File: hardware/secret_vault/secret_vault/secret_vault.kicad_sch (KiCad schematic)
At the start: 13 parts

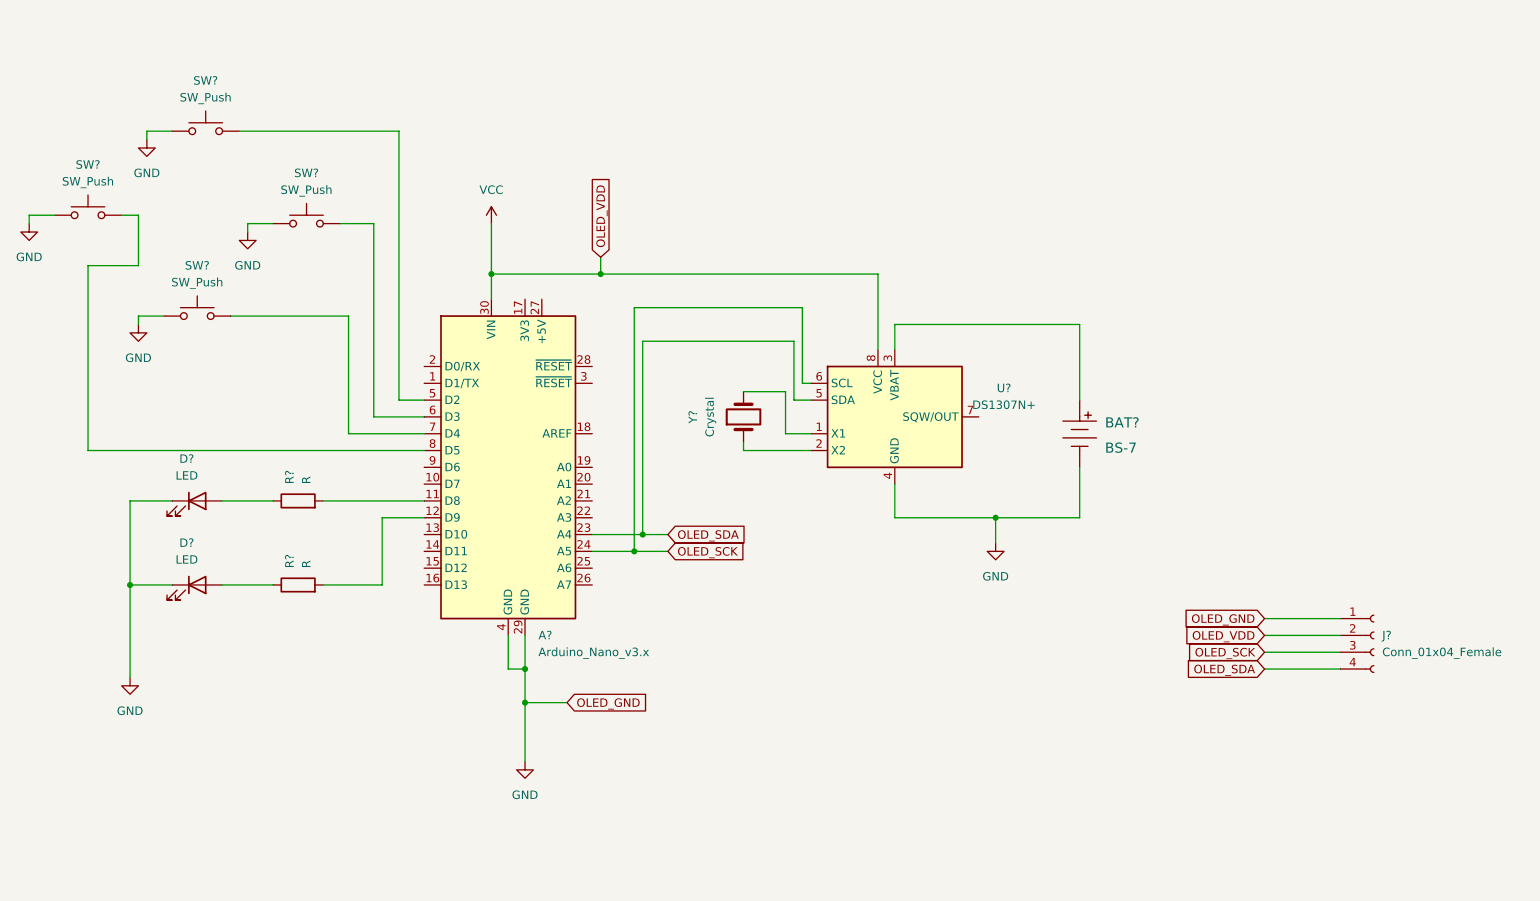
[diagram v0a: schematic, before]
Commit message: Updated PCB board and sent it to OSH park for fab
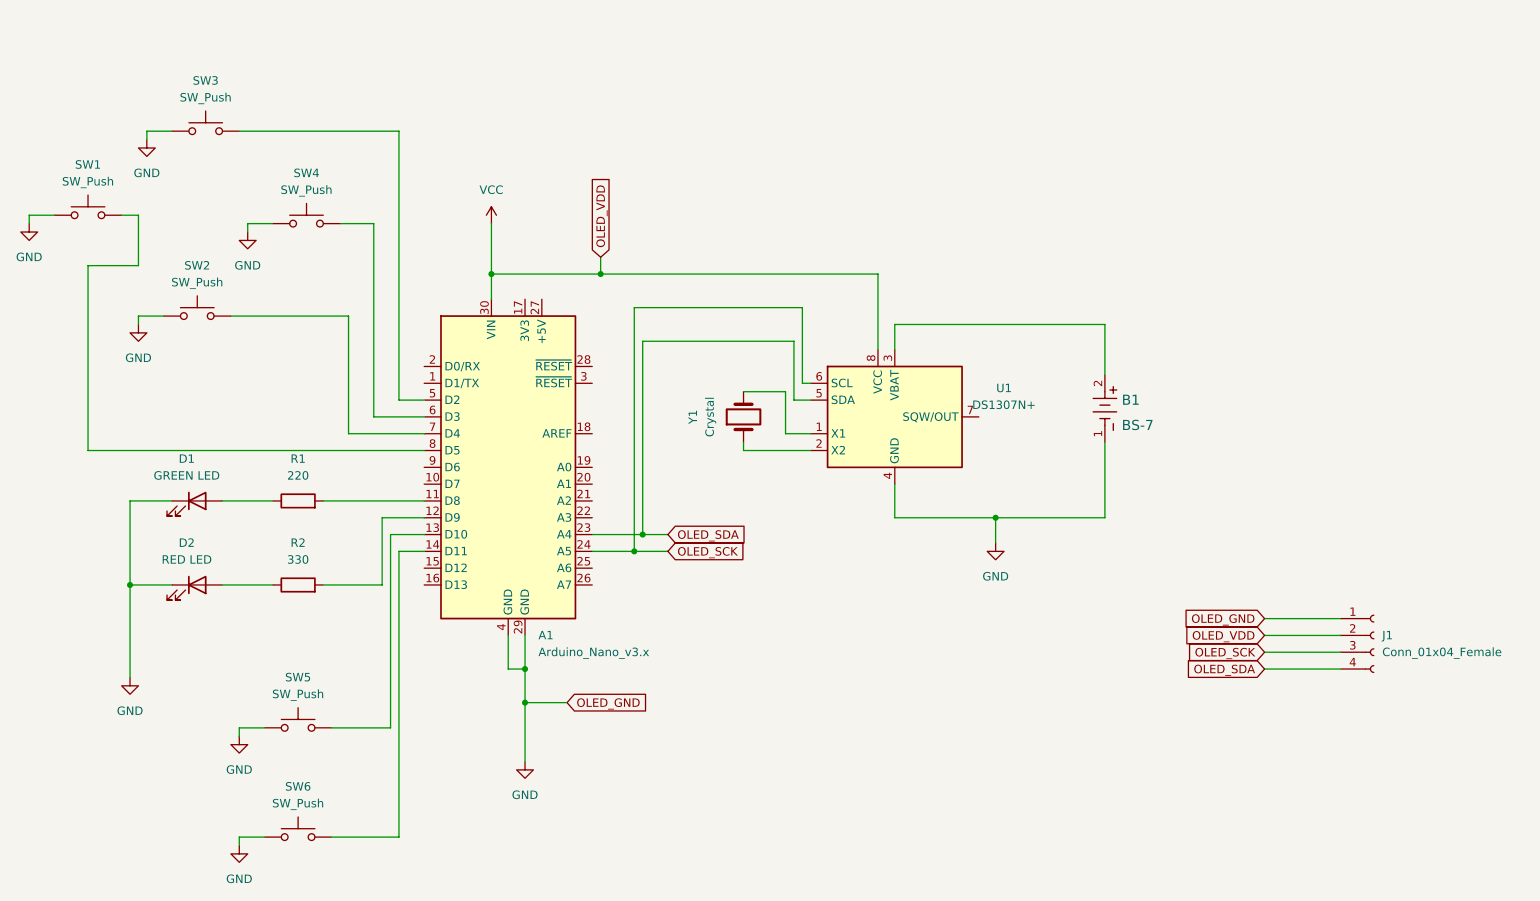
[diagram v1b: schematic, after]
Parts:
- removed BAT?: BS-7, digikey-footprints:Battery_Holder_Coin_2032_BS-7, symbol dk battery:BS-7
- added B1: BS-7, bs7batt:BS-7_MPD, symbol custombattery:BS-7
- added SW5, SW6: SW_Push, Button_Switch_THT:SW_TH_Tactile_Omron_B3F-10xx, symbol Switch:SW_Push
- D1: renamed from D?; value LED -> GREEN LED; footprint (none) -> LED_THT:LED_D5.0mm
- D2: renamed from D?; value LED -> RED LED; footprint (none) -> LED_THT:LED_D5.0mm
- R1: renamed from R?; value R -> 220; footprint (none) -> Resistor_THT:R_Axial_DIN0207_L6.3mm_D2.5mm_P7.62mm_Horizontal
- R2: renamed from R?; value R -> 330; footprint (none) -> Resistor_THT:R_Axial_DIN0207_L6.3mm_D2.5mm_P7.62mm_Horizontal
- SW1, SW2, SW3, SW4: renamed from SW?; footprint (none) -> Button_Switch_THT:SW_TH_Tactile_Omron_B3F-10xx
- Y1: renamed from Y?; footprint (none) -> Crystal:Crystal_C26-LF_D2.1mm_L6.5mm_Horizontal
- gave numbers to parts that had none: 3
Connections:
- net GND: now also B1.1, SW5.1, SW6.1
- net at A1.13 (D10): now also SW5.2
- net at A1.14 (D11): now also SW6.2
- net at U1.3 (VBAT): now also B1.2

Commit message: Many fixes to the v0.2 secret vault board
- Added pullup resistor for I2C lines
- All of the switch footprints were wrong
- RTC Vcc tied to 5V instead of Vin
- Added QR code to silkscreen
- Made the resistors a larger part
- Enlarged many of the fonts
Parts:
- added R3, R4: 2.2K, Resistor_THT:R_Axial_DIN0309_L9.0mm_D3.2mm_P12.70mm_Horizontal, symbol Device:R
- R1, R2: footprint Resistor_THT:R_Axial_DIN0207_L6.3mm_D2.5mm_P7.62mm_Horizontal -> Resistor_THT:R_Axial_DIN0309_L9.0mm_D3.2mm_P12.70mm_Horizontal
- SW1, SW2, SW3, SW4, SW5, SW6: footprint Button_Switch_THT:SW_TH_Tactile_Omron_B3F-10xx -> cust_sw:SW_TH_Tactile_Omron_B3F-10xx_stackedpninums
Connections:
- net OLED_SCK: now also R3.2
- net OLED_SDA: now also R4.2
- net VCC: now also A1.27 (+5V), R3.1, R4.1; no longer A1.30 (VIN)
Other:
- moved on the sheet: A1, B1, D1, D2, R1, R2, SW1, SW2, SW3, SW4, SW5, SW6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
